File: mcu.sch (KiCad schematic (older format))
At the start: 18 parts, among them J501 JTAG, J502 Serial / Bootloader, SW501 EVQQ2, SW502 EVQQ2, U501 STM32F405RGTx, Y501 8MHz

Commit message: only ground plane left
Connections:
- net CLK_IN: now also U501.30 (ADC1_EXTI11/ADC2_EXTI11/ADC3_EXTI11/I2C2_SDA/TIM2_CH4/USART3_RX/USB_OTG_HS_ULPI_D4/PB11)
- net CLK_OUT: now also U501.28 (BOOT1/PB2)
- net RES_IN: now also U501.29 (I2C2_SCL/I2S2_CK/SPI2_SCK/TIM2_CH3/USART3_TX/USB_OTG_HS_ULPI_D3/PB10)
- net RES_OUT: now also U501.27 (ADC1_IN9/ADC2_IN9/TIM1_CH3N/TIM3_CH4/TIM8_CH3N/USB_OTG_HS_ULPI_D2/PB1)
- net SR_LATCH: now also U501.25 (PC5/ADC1_IN15/ADC2_IN15); no longer U501.26 (ADC1_IN8/ADC2_IN8/TIM1_CH2N/TIM3_CH3/TIM8_CH2N/USB_OTG_HS_ULPI_D1/PB0)
- net SR_LOAD: now also U501.24 (PC4/ADC1_IN14/ADC2_IN14); no longer U501.27 (ADC1_IN9/ADC2_IN9/TIM1_CH3N/TIM3_CH4/TIM8_CH3N/USB_OTG_HS_ULPI_D2/PB1)
- net USB_PWR_EN: now also U501.40 (PC9/DAC_EXTI9/I2C3_SDA/I2S_CKIN/RCC_MCO_2/SDIO_D1/TIM3_CH4/TIM8_CH4)
- net USB_PWR_FAULT: now also U501.41 (I2C3_SCL/RCC_MCO_1/TIM1_CH1/USART1_CK/USB_OTG_FS_SOF/PA8)
- net SPI2_MISO: no longer names the net of U501.10 (PC2/ADC1_IN12/ADC2_IN12/ADC3_IN12/I2S2_ext_SD/SPI2_MISO/USB_OTG_HS_ULPI_DIR)
- net SPI3_MISO: no longer names the net of U501.52 (PC11/ADC1_EXTI11/ADC2_EXTI11/ADC3_EXTI11/I2S3_ext_SD/SDIO_D3/SPI3_MISO/UART4_RX/USART3_RX)
- new net DAC_SYNC: U501.26 (ADC1_IN8/ADC2_IN8/TIM1_CH2N/TIM3_CH3/TIM8_CH2N/USB_OTG_HS_ULPI_D1/PB0)
- no-connect marks 5 -> 7
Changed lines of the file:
@@
 $EndComp
 $Comp
-L GND #PWR507
+L GND #PWR050
 U 1 1 59DB9615
 P 1600 6200
-F 0 "#PWR507" H 1600 5950 50  0001 C CNN
+F 0 "#PWR050" H 1600 5950 50  0001 C CNN
 F 1 "GND" H 1600 6050 50  0000 C CNN
 F 2 "" H 1600 6200 50  0001 C CNN
@@
 $EndComp
 $Comp
-L +3.3V #PWR505
+L +3.3V #PWR051
 U 1 1 59DB9CCC
 P 2500 5500
-F 0 "#PWR505" H 2500 5350 50  0001 C CNN
+F 0 "#PWR051" H 2500 5350 50  0001 C CNN
 F 1 "+3.3V" H 2500 5640 50  0000 C CNN
 F 2 "" H 2500 5500 50  0001 C CNN
@@
 $EndComp
 $Comp
-L GND #PWR506
+L GND #PWR052
 U 1 1 59DB9CF4
 P 2500 6100
-F 0 "#PWR506" H 2500 5850 50  0001 C CNN
+F 0 "#PWR052" H 2500 5850 50  0001 C CNN
 F 1 "GND" H 2500 5950 50  0000 C CNN
 F 2 "" H 2500 6100 50  0001 C CNN
@@
 $EndComp
 $Comp
-L +3.3V #PWR501
+L +3.3V #PWR053
 U 1 1 59DB9EAC
 P 5500 1000
-F 0 "#PWR501" H 5500 850 50  0001 C CNN
+F 0 "#PWR053" H 5500 850 50  0001 C CNN
 F 1 "+3.3V" H 5500 1140 50  0000 C CNN
 F 2 "" H 5500 1000 50  0001 C CNN
@@
 $EndComp
 $Comp
-L +3.3VA #PWR502
+L +3.3VA #PWR054
 U 1 1 59DB9EE7
 P 6000 1000
-F 0 "#PWR502" H 6000 850 50  0001 C CNN
+F 0 "#PWR054" H 6000 850 50  0001 C CNN
 F 1 "+3.3VA" H 6000 1140 50  0000 C CNN
 F 2 "" H 6000 1000 50  0001 C CNN
@@
 $EndComp
 $Comp
-L GND #PWR504
+L GND #PWR055
 U 1 1 59DB9FE7
 P 5800 5400
-F 0 "#PWR504" H 5800 5150 50  0001 C CNN
+F 0 "#PWR055" H 5800 5150 50  0001 C CNN
 F 1 "GND" H 5800 5250 50  0000 C CNN
 F 2 "" H 5800 5400 50  0001 C CNN
@@
 $EndComp
 $Comp
-L GND #PWR512
+L GND #PWR056
 U 1 1 59DBA437
 P 800 7300
-F 0 "#PWR512" H 800 7050 50  0001 C CNN
+F 0 "#PWR056" H 800 7050 50  0001 C CNN
 F 1 "GND" H 800 7150 50  0000 C CNN
 F 2 "" H 800 7300 50  0001 C CNN
@@
 $EndComp
 $Comp
-L GND #PWR503
+L GND #PWR057
 U 1 1 59DBB736
 P 800 2250
-F 0 "#PWR503" H 800 2000 50  0001 C CNN
+F 0 "#PWR057" H 800 2000 50  0001 C CNN
 F 1 "GND" H 800 2100 50  0000 C CNN
 F 2 "" H 800 2250 50  0001 C CNN
@@
 $EndComp
 $Comp
-L +3.3V #PWR508
+L +3.3V #PWR058
 U 1 1 59DD49A9
 P 5900 6300
-F 0 "#PWR508" H 5900 6150 50  0001 C CNN
+F 0 "#PWR058" H 5900 6150 50  0001 C CNN
 F 1 "+3.3V" H 5900 6440 50  0000 C CNN
 F 2 "" H 5900 6300 50  0001 C CNN
@@
 $EndComp
 $Comp
-L +3.3V #PWR509
+L +3.3V #PWR059
 U 1 1 59DD49E1
 P 6500 6300
-F 0 "#PWR509" H 6500 6150 50  0001 C CNN
+F 0 "#PWR059" H 6500 6150 50  0001 C CNN
 F 1 "+3.3V" H 6500 6440 50  0000 C CNN
 F 2 "" H 6500 6300 50  0001 C CNN
@@
 $EndComp
 $Comp
-L GND #PWR513
+L GND #PWR060
 U 1 1 59DD4A83
 P 5900 7400
-F 0 "#PWR513" H 5900 7150 50  0001 C CNN
+F 0 "#PWR060" H 5900 7150 50  0001 C CNN
 F 1 "GND" H 5900 7250 50  0000 C CNN
 F 2 "" H 5900 7400 50  0001 C CNN
@@
 $EndComp
 $Comp
-L GND #PWR514
+L GND #PWR061
 U 1 1 59DD4ABB
 P 6500 7400
-F 0 "#PWR514" H 6500 7150 50  0001 C CNN
+F 0 "#PWR061" H 6500 7150 50  0001 C CNN
 F 1 "GND" H 6500 7250 50  0000 C CNN
 F 2 "" H 6500 7400 50  0001 C CNN
@@
 $EndComp
 $Comp
-L +3.3V #PWR510
+L +3.3V #PWR062
 U 1 1 59E34B90
 P 2500 6800
-F 0 "#PWR510" H 2500 6650 50  0001 C CNN
+F 0 "#PWR062" H 2500 6650 50  0001 C CNN
 F 1 "+3.3V" H 2500 6940 50  0000 C CNN
 F 2 "" H 2500 6800 50  0001 C CNN
@@
 $EndComp
 $Comp
-L GND #PWR515
+L GND #PWR063
 U 1 1 59E34BD4
 P 2500 7500
-F 0 "#PWR515" H 2500 7250 50  0001 C CNN
+F 0 "#PWR063" H 2500 7250 50  0001 C CNN
 F 1 "GND" H 2500 7350 50  0000 C CNN
 F 2 "" H 2500 7500 50  0001 C CNN
@@
 $EndComp
 $Comp
-L +3.3VA #PWR511
+L +3.3VA #PWR064
 U 1 1 59E35078
 P 3900 6800
-F 0 "#PWR511" H 3900 6650 50  0001 C CNN
+F 0 "#PWR064" H 3900 6650 50  0001 C CNN
 F 1 "+3.3VA" H 3900 6940 50  0000 C CNN
 F 2 "" H 3900 6800 50  0001 C CNN
@@
 $EndComp
 $Comp
-L GND #PWR516
+L GND #PWR065
 U 1 1 59E350BC
 P 3900 7500
-F 0 "#PWR516" H 3900 7250 50  0001 C CNN
+F 0 "#PWR065" H 3900 7250 50  0001 C CNN
 F 1 "GND" H 3900 7350 50  0000 C CNN
 F 2 "" H 3900 7500 50  0001 C CNN
@@
 Text GLabel 1400 4800 0    51   Input ~ 0
 ENC_SW
-Text GLabel 1400 3500 0    51   Input ~ 0
-SPI2_MISO
-Text GLabel 900  3600 0    51   Output ~ 0
-SPI2_MOSI
-Text GLabel 10700 4600 2    51   Output ~ 0
-SPI2_SCK
-Text GLabel 10700 3800 2    51   Output ~ 0
-SPI3_MOSI
-Text GLabel 900  4300 0    51   Output ~ 0
-SPI3_SCK
-Text GLabel 1400 4400 0    51   Input ~ 0
-SPI3_MISO
 Text GLabel 10200 1600 2    51   Input ~ 0
 CV1_IN
@@
 Text GLabel 10200 1900 2    51   Input ~ 0
 CV4_IN
-Text GLabel 7000 5600 2    51   Output ~ 0
+Text GLabel 10200 3500 2    51   Output ~ 0
 CLK_OUT
-Text GLabel 7000 5700 2    51   Output ~ 0
+Text GLabel 10200 3400 2    51   Output ~ 0
 RES_OUT
-Text GLabel 7000 5800 2    51   Input ~ 0
+Text GLabel 10200 4400 2    51   Input ~ 0
 CLK_IN
-Text GLabel 7000 5900 2    51   Input ~ 0
+Text GLabel 10200 4300 2    51   Input ~ 0
 RES_IN
 Text GLabel 10200 2300 2    51   Output ~ 0
@@
 Text GLabel 10200 2100 2    51   Output ~ 0
 SR_SCK
-Text GLabel 10200 3300 2    51   Output ~ 0
+Text GLabel 1400 3800 0    51   Output ~ 0
 SR_LATCH
-Text GLabel 10200 3400 2    51   Output ~ 0
+Text GLabel 1400 3700 0    51   Output ~ 0
 SR_LOAD
 Text GLabel 10200 3800 2    51   Output ~ 0
@@
 Text GLabel 1400 4300 0    51   Output ~ 0
 DAC_SCK
-Text GLabel 7800 5600 2    51   Output ~ 0
+Text GLabel 1400 4200 0    51   Output ~ 0
 USB_PWR_EN
-Text GLabel 7800 5700 2    51   Input ~ 0
+Text GLabel 10200 2400 2    51   Input ~ 0
 USB_PWR_FAULT
 Text GLabel 10200 2700 2    51   Output ~ 0
@@
 	10100 3600 10200 3600
 Wire Wire Line
-	1500 2100 1400 2100
-Wire Wire Line
-	1400 2100 1400 2050
+	1400 2100 1500 2100
+Wire Wire Line
+	1400 2000 1400 2100
 Wire Wire Line
 	1400 2050 1300 2050
@@
 	1500 2200 1400 2200
 Wire Wire Line
-	1400 2200 1400 2250
+	1400 2200 1400 2300
 Wire Wire Line
 	1400 2250 1300 2250
@@
 	10100 2300 10200 2300
 Wire Wire Line
-	1500 3500 1400 3500
-Wire Wire Line
 	1500 3600 1400 3600
 Wire Wire Line
@@
 Wire Wire Line
 	1400 4300 1500 4300
-Wire Wire Line
-	1400 4400 1500 4400
 Wire Wire Line
 	10100 1600 10200 1600
@@
 NoConn ~ 2600 5900
 NoConn ~ 1500 2000
+Text GLabel 10200 3300 2    51   Output ~ 0
+DAC_SYNC
+Wire Wire Line
+	1400 3700 1500 3700
+Wire Wire Line
+	1400 3800 1500 3800
+Wire Wire Line
+	10100 3500 10200 3500
+Wire Wire Line
+	10100 4300 10200 4300
+NoConn ~ 1500 3500
+NoConn ~ 1500 4400
+Wire Wire Line
+	10200 4400 10100 4400
+Wire Wire Line
+	10200 2400 10100 2400
+Wire Wire Line
+	1400 4200 1500 4200
+$Comp
+L PWR_FLAG #FLG066
+U 1 1 59F48B1D
+P 1400 2300
+F 0 "#FLG066" H 1400 2375 50  0001 C CNN
+F 1 "PWR_FLAG" H 1400 2450 50  0001 C CNN
+F 2 "" H 1400 2300 50  0001 C CNN
+F 3 "" H 1400 2300 50  0001 C CNN
+	1    1400 2300
+	-1   0    0    1
+$EndComp
+Connection ~ 1400 2250
+$Comp
+L PWR_FLAG #FLG067
+U 1 1 59F48C86
+P 1400 2000
+F 0 "#FLG067" H 1400 2075 50  0001 C CNN
+F 1 "PWR_FLAG" H 1400 2150 50  0001 C CNN
+F 2 "" H 1400 2000 50  0001 C CNN
+F 3 "" H 1400 2000 50  0001 C CNN
+	1    1400 2000
+	1    0    0    -1
+$EndComp
+Connection ~ 1400 2050
 $EndSCHEMATC

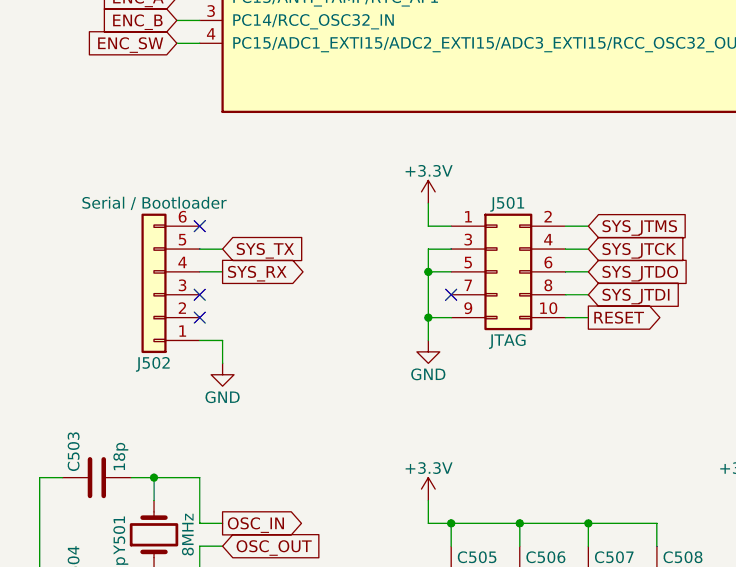
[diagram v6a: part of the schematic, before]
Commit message: renamed header references to JPxxx
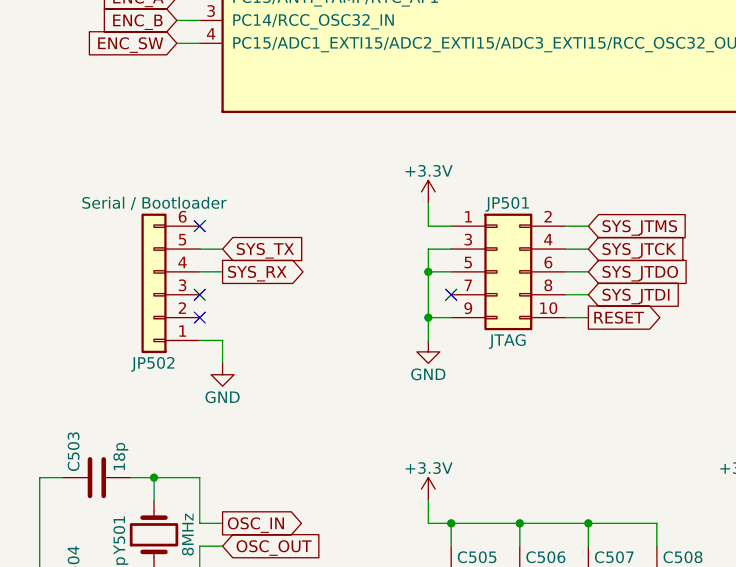
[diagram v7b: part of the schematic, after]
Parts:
- renumbered J501 to JP501, J502 to JP502
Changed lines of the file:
@@
 $EndComp
 $Comp
-L Conn_01x06 J502
+L Conn_01x06 JP502
 U 1 1 59DB9577
 P 1300 5900
-F 0 "J502" H 1300 6200 50  0000 C CNN
+F 0 "JP502" H 1300 6200 50  0000 C CNN
 F 1 "Serial / Bootloader" H 1300 5500 50  0000 C CNN
 F 2 "Pin_Headers:Pin_Header_Straight_1x06_Pitch2.54mm" H 1300 5900 50  0001 C CNN
@@
 $EndComp
 $Comp
-L Conn_02x05_Odd_Even J501
+L Conn_02x05_Odd_Even JP501
 U 1 1 59DB9B82
 P 2800 5800
-F 0 "J501" H 2850 6100 50  0000 C CNN
+F 0 "JP501" H 2850 6100 50  0000 C CNN
 F 1 "JTAG" H 2850 5500 50  0000 C CNN
 F 2 "Pin_Headers:Pin_Header_Straight_2x05_Pitch1.27mm" H 2800 5800 50  0001 C CNN

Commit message: last minute fixes
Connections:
- no-connect marks 7 -> 15
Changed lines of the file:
@@
 $EndComp
 Connection ~ 1400 2050
+NoConn ~ 10100 4200
+NoConn ~ 10100 4100
+NoConn ~ 10100 4000
+NoConn ~ 10100 3900
+NoConn ~ 10100 3700
+NoConn ~ 10100 2000
+NoConn ~ 1500 3300
+NoConn ~ 1500 3400
 $EndSCHEMATC
